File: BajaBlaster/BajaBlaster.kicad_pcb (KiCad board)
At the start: 4 copper layers, 59.2 x 47.5 mm, 51 parts, among them J201 Conn_01x02_Pin, J501 Conn_01x06_Pin, J502 INTERBOARD, J503 Conn_01x04_Pin, SW301 SW_Push, SW302 SW_Push, U201 AP2112K-3.3, U202 TPS562200, U301 ESP32-WROOM-32, U302 MPU-6050, U501 TCAN330

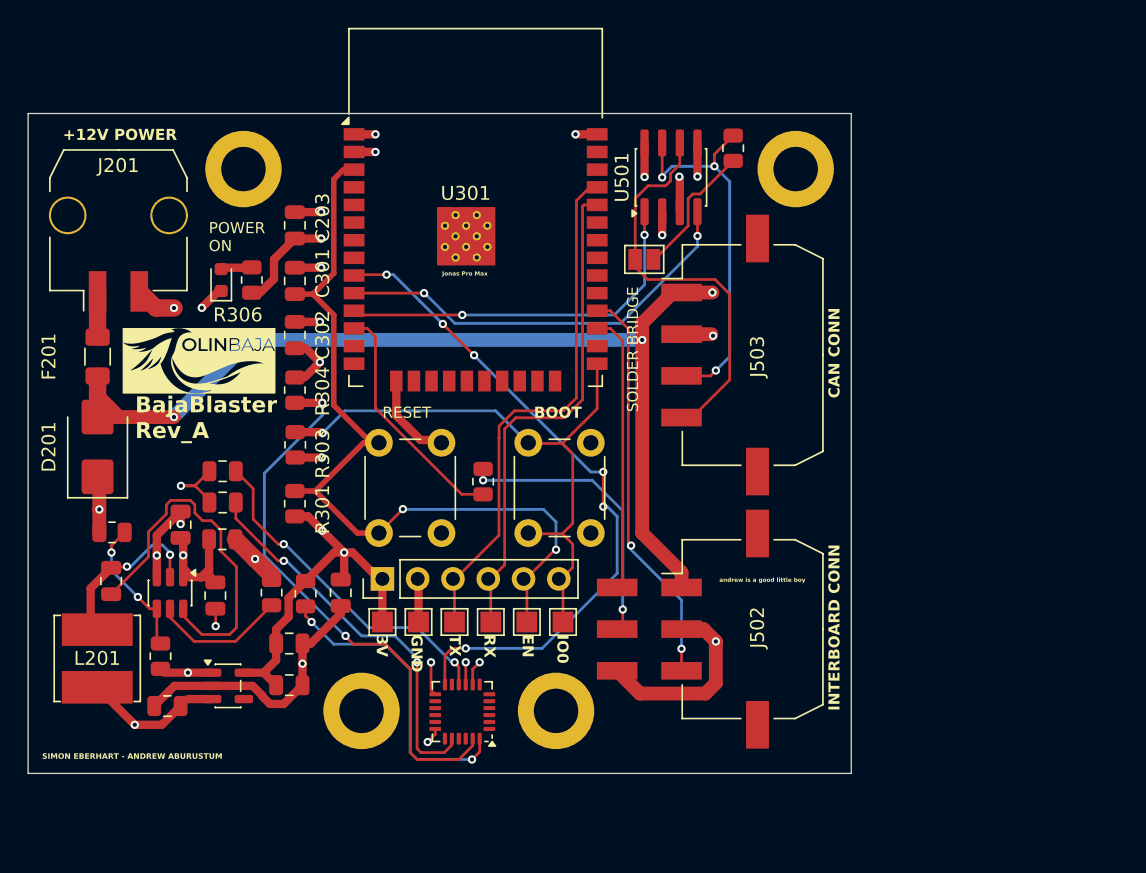
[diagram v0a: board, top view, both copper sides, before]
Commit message: fixed a bunch of smal stuff including changing the cap to be the correct footprint
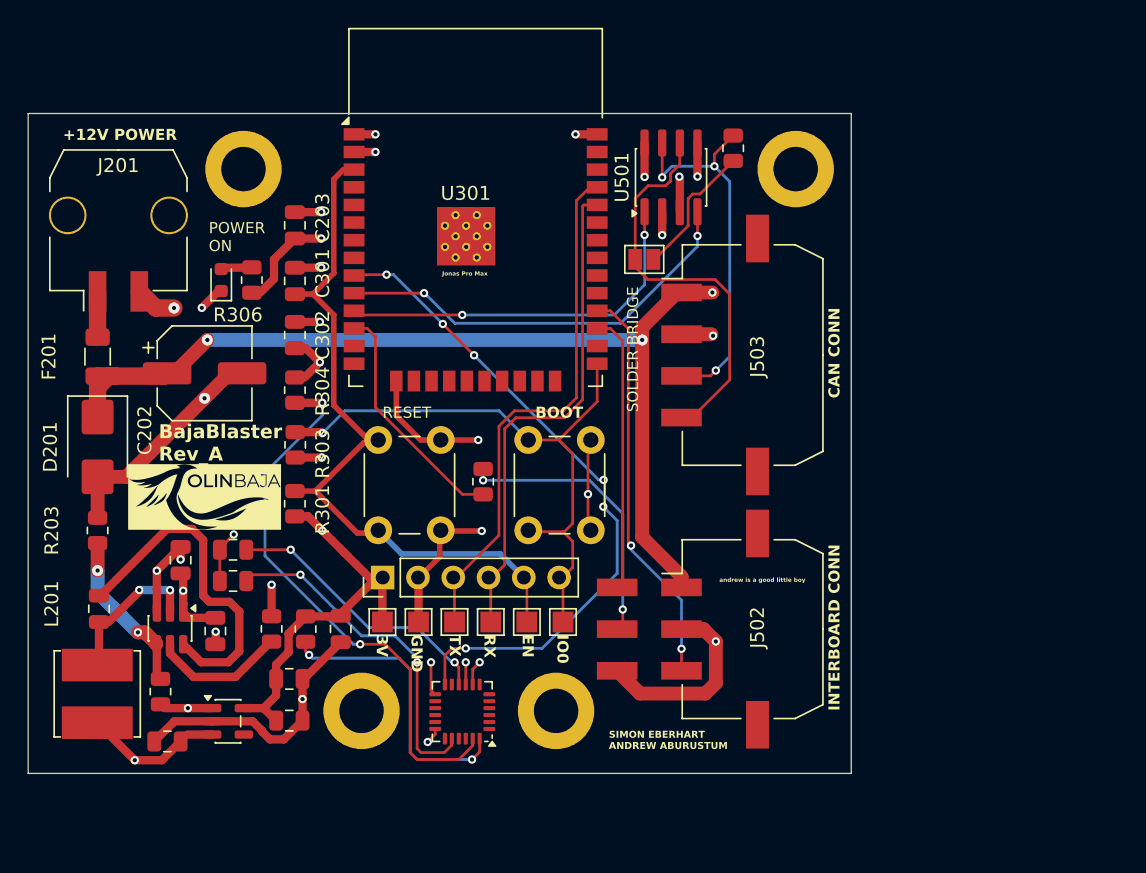
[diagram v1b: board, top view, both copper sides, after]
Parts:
- C202: footprint Capacitor_SMD:C_0805_2012Metric -> Capacitor_SMD:CP_Elec_6.3x7.7
- D201: value SMBJ24A -> SMBJ12A
- L201: value 22uH -> 4.7uH
- moved C202 12.0 mm to (37.7, 93.7)
- moved G*** 9.81 mm to (37.7, 102.6)
- moved C305 5.70 mm to (39.8, 106.4)
- moved C306 5.70 mm to (39.8, 108.7)
- moved R201 2.61 mm to (42.5, 112.1)
- moved C303 2.60 mm to (47.5, 112.1)
- moved C204 2.55 mm to (36.0, 107.2)
- moved L201 2.55 mm to (30.0, 116.8)
- moved C201 2.55 mm to (38.5, 112.2)
- moved C205 2.55 mm to (35.0, 120.2)
- moved C304 2.55 mm to (43.8, 115.7)
- moved C501 2.55 mm to (43.8, 118.7)
- moved R202 2.55 mm to (34.5, 116.6)
- moved R305 2.55 mm to (45.0, 112.1)
- moved U201 2.55 mm to (39.4, 118.8)
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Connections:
- C202 pad 1: GND -> +12V
- C202 pad 2: +12V -> GND
- D201 pad 1: GND -> +12V
- D201 pad 2: +12V -> GND
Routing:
- net GND: track 87.4 -> 109.7 mm, vias 18 -> 21
- net /COMMS/ESP32_EN: track 59.4 -> 54.3 mm, vias 2 -> 0
- net Net-(U302-REGOUT): track 24.5 -> 20.1 mm
- net Net-(U302-CPOUT): track 28.2 -> 24.8 mm
- net +12V: track 82.4 -> 79.2 mm
- net Net-(U202-VFB): track 9.78 -> 11.6 mm
- net +3V3: track 48.6 -> 50.0 mm, vias 9 -> 8
- net Net-(U302-SDA): track 22.2 -> 21.1 mm
- net Net-(U202-VBST): track 25.4 -> 24.7 mm
- net /COMMS/IO0: track 43.7 -> 43.2 mm
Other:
- board text added: "SIMON EBERHART ANDREW ABURUSTUM"
- board text removed: "SIMON EBERHART - ANDREW ABURUSTUM"

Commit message: good for fab
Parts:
- moved C202 0.32 mm to (38.0, 93.6)
- moved D301 0.20 mm to (38.9, 86.8)
- moved R306 0.20 mm to (41.1, 86.8)
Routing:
- net +3V3: track 50.0 -> 50.6 mm
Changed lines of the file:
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@@
 	(footprint "Capacitor_SMD:CP_Elec_6.3x7.7"
 		(layer "F.Cu")
-		(at 37.7 93.7)
+		(at 38 93.6)
 		(descr "SMD capacitor, aluminum electrolytic, Nichicon, 6.3x7.7mm")
 		(tags "capacitor electrolytic")
 		(property "Reference" "C202"
-			(at -4.3 4.1 90)
+			(at -4.5 4.1 90)
 			(layer "F.SilkS")
 			(effects
@@
 	(footprint "Resistor_SMD:R_0805_2012Metric"
 		(layer "F.Cu")
-		(at 41.1 86.9875 90)
+		(at 41.1 86.7875 90)
 		(descr "Resistor SMD 0805 (2012 Metric), square (rectangular) end terminal, IPC-7351 nominal, (Body size source: IPC-SM-782 page 72, https://www.pcb-3d.com/wordpress/wp-content/uploads/ipc-sm-782a_amendment_1_and_2.pdf)")
 		(tags "resistor")
@@
 	(footprint "LED_SMD:LED_0603_1608Metric"
 		(layer "F.Cu")
-		(at 38.9 86.9875 90)
+		(at 38.9 86.7875 90)
 		(descr "LED SMD 0603 (1608 Metric), square (rectangular) end terminal, IPC-7351 nominal, (Body size source: http://www.tortai-tech.com/upload/download/2011102023233369053.pdf)")
 		(tags "LED")
@@
 	)
 	(gr_rect
+		(start 32.199253 104.962389)
+		(end 43.2 105.1)
+		(stroke
+			(width 0)
+			(type solid)
+		)
+		(fill yes)
+		(layer "F.SilkS")
+	)
+	(gr_rect
+		(start 39.912942 100.9)
+		(end 43.076959 101.898755)
+		(stroke
+			(width 0.2)
+			(type solid)
+		)
+		(fill yes)
+		(layer "F.SilkS")
+	)
+	(gr_rect
 		(start 25 75)
 		(end 84.25 122.5)
@@
 	)
 	(segment
+		(start 65.3 103.3)
+		(end 65.3 98.8)
+		(width 0.2)
+		(layer "F.Cu")
+		(net "GND")
+	)
+	(segment
 		(start 38.25 118.75)
 		(end 35.525 118.75)
@@
 	)
 	(segment
+		(start 65.3 105.1)
+		(end 65.3 103.3)
+		(width 0.2)
+		(layer "F.Cu")
+		(net "GND")
+	)
+	(segment
 		(start 34.195 89)
 		(end 33 87.805)
@@
 	)
 	(segment
-		(start 65.3 105.1)
-		(end 65.3 102.4)
-		(width 0.2)
-		(layer "F.Cu")
-		(net "GND")
-	)
-	(segment
 		(start 36.1625 110.25)
 		(end 36.1625 110.2875)
@@
 	)
 	(segment
-		(start 65.3 102.4)
-		(end 65.3 98.8)
-		(width 0.2)
-		(layer "F.Cu")
-		(net "GND")
-	)
-	(segment
 		(start 74.5 116)
 		(end 73.75 116.75)
@@
 	)
 	(segment
+		(start 37.2875 89)
+		(end 38.7125 87.575)
+		(width 0.6)
+		(layer "F.Cu")
+		(net "GND")
+	)
+	(segment
 		(start 38.8 106.3)
 		(end 38.8 106.4)
@@
 	)
 	(segment
-		(start 38.7125 87.775)
-		(end 37.5 88.9875)
-		(width 0.6)
-		(layer "F.Cu")
-		(net "GND")
-	)
-	(segment
 		(start 65.96 76.5)
 		(end 64.4 76.5)
@@
 	)
 	(via
-		(at 37.5 88.9875)
+		(at 37.2875 89)
 		(size 0.6)
 		(drill 0.3)
@@
 	)
 	(via
-		(at 65.3 102.4)
+		(at 65.3 103.3)
 		(size 0.6)
 		(drill 0.3)
@@
 	)
 	(segment
+		(start 42.7 86.9)
+		(end 41.9 87.7)
+		(width 0.6)
+		(layer "F.Cu")
+		(net "+3V3")
+	)
+	(segment
 		(start 45.15 104)
 		(end 46.175 105.025)
@@
 	)
 	(segment
-		(start 44.975 111.244912)
-		(end 44.975 111.2)
+		(start 41.9 87.7)
+		(end 41.1 87.7)
 		(width 0.6)
 		(layer "F.Cu")
@@
 	)
 	(segment
-		(start 41.7 87.9)
-		(end 42.7 86.9)
+		(start 44.975 111.244912)
+		(end 44.975 111.2)
 		(width 0.6)
 		(layer "F.Cu")
@@
 	)
 	(segment
-		(start 34.2625 109.2125)
-		(end 34.275 109.2)
-		(width 0.2)
-		(layer "F.Cu")
-		(net "+12V")
-	)
-	(segment
 		(start 42.525 108.925)
 		(end 42.5 108.9)
@@
 	)
 	(segment
-		(start 39 86.1)
-		(end 41.075 86.1)
+		(start 39 85.9)
+		(end 41.075 85.9)
 		(width 0.6)
 		(layer "F.Cu")
@@
 	)
 	(segment
-		(start 57.75 100.5875)
-		(end 57.75 101.4)
+		(start 57.75 101.384913)
+		(end 57.765087 101.4)
 		(width 0.2)
 		(layer "F.Cu")
@@
 	)
 	(segment
-		(start 57.75 101.4)
+		(start 57.75 101.415087)
 		(end 57.75 101.55)
 		(width 0.2)
@@
 	)
 	(segment
+		(start 57.765087 101.4)
+		(end 57.75 101.415087)
+		(width 0.2)
+		(layer "F.Cu")
+		(net "/COMMS/SYNC")
+	)
+	(segment
+		(start 57.75 100.5875)
+		(end 57.75 101.384913)
+		(width 0.2)
+		(layer "F.Cu")
+		(net "/COMMS/SYNC")
+	)
+	(segment
 		(start 67.8 110.7)
 		(end 67.8 111.715)
@@
 	)
 	(via
-		(at 57.75 101.4)
+		(at 57.765087 101.4)
 		(size 0.6)
 		(drill 0.3)
@@
 	)
 	(segment
-		(start 67.8 110.7)
+		(start 65.4 101.4)
 		(end 67.8 103.8)
 		(width 0.2)
@@
 	)
 	(segment
-		(start 67.8 103.8)
+		(start 57.765087 101.4)
 		(end 65.4 101.4)
 		(width 0.2)
@@
 	)
 	(segment
-		(start 65.4 101.4)
-		(end 57.75 101.4)
+		(start 67.8 103.8)
+		(end 67.8 110.7)
 		(width 0.2)
 		(layer "B.Cu")

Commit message: sendoff
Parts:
- removed R302: 50 OHM, Resistor_SMD:R_0805_2012Metric
- removed SW301, SW302: SW_Push, Button_Switch_THT:SW_PUSH_6mm
- removed U301: ESP32-WROOM-32, RF_Module:ESP32-WROOM-32
- added C302: 10pF, Capacitor_SMD:C_0805_2012Metric, F.Cu at (41.0, 88.5)
- added C303: 100nF, Capacitor_SMD:C_0805_2012Metric, F.Cu at (44.2, 91.0)
- added C307: 10uF, Capacitor_SMD:C_0805_2012Metric, F.Cu at (44.2, 87.0)
- added C308: 100nF, Capacitor_SMD:C_0805_2012Metric, F.Cu at (46.4, 87.0)
- added C309: 100nF, Capacitor_SMD:C_0805_2012Metric, F.Cu at (101.2, 85.8)
- added C310: 10uF, Capacitor_SMD:C_0805_2012Metric, F.Cu at (91.0, 94.0)
- added C311: 100nF, Capacitor_SMD:C_0805_2012Metric, F.Cu at (47.1, 83.6)
- added C312: 4.7uF, Capacitor_SMD:C_0805_2012Metric, F.Cu at (62.8, 94.6)
- added C313: 100nF, Capacitor_SMD:C_0805_2012Metric, F.Cu at (90.2, 101.0)
- added C502: 100nf, Capacitor_SMD:C_0805_2012Metric, F.Cu at (47.4, 95.4)
- added C503: 47pF 50V, Capacitor_SMD:C_0805_2012Metric, F.Cu at (62.8, 88.0)
- added C504: 47pF 50V, Capacitor_SMD:C_0805_2012Metric, F.Cu at (62.8, 85.8)
- added C505: 47pF 50V, Capacitor_SMD:C_0805_2012Metric, F.Cu at (62.8, 83.6)
- added C506: 47pF 50V, Capacitor_SMD:C_0805_2012Metric, F.Cu at (66.7, 89.0)
- added C507: 47pF 50V, Capacitor_SMD:C_0805_2012Metric, F.Cu at (62.8, 90.2)
- added C508: 47pF 50V, Capacitor_SMD:C_0805_2012Metric, F.Cu at (74.8, 78.4)
- added C509: 47pF 50V, Capacitor_SMD:C_0805_2012Metric, F.Cu at (66.7, 111.8)
- added C510: 47pF 50V, Capacitor_SMD:C_0805_2012Metric, F.Cu at (66.7, 109.6)
- added D501: NUP2105L, Package_TO_SOT_SMD:SOT-23, F.Cu at (66.5, 91.8)
- added D502: NUP2105L, Package_TO_SOT_SMD:SOT-23, F.Cu at (66.5, 104.0)
- added FL501: 1812CAN-513NRC, Inductor_SMD:L_CommonModeChoke_Coilcraft_1812CAN, F.Cu at (71.7, 79.3)
- added FL502: 1812CAN-513NRC, Inductor_SMD:L_CommonModeChoke_Coilcraft_1812CAN, F.Cu at (55.0, 79.4)
- added J504: Conn_01x04_Pin, Connector_JST:JST_JWPF_B04B-JWPF-SK-R_1x04_P2.00mm_Vertical, F.Cu at (74.5, 111.0)
- added JP502: SolderJumper_2_Open, Jumper:SolderJumper-2_P1.3mm_Open_Pad1.0x1.5mm, F.Cu at (66.7, 86.6)
- added JP503: JP_EXT_PWR, Jumper:SolderJumper-2_P1.3mm_Open_Pad1.0x1.5mm, F.Cu at (66.7, 84.0)
- added R303: 10kOHM, Resistor_SMD:R_0805_2012Metric, F.Cu at (44.2, 102.8)
- added R309: 10kOHM, Resistor_SMD:R_0805_2012Metric, F.Cu at (44.2, 107.0)
- added R_CAN_TERM502: 120 OHM, Resistor_SMD:R_0805_2012Metric, F.Cu at (66.7, 94.6)
- added SW303: SW_Push, Button_Switch_THT:SW_PUSH_6mm, F.Cu at (48.1, 105.2)
- added SW305: SW_Push, Button_Switch_THT:SW_PUSH_6mm, F.Cu at (55.8, 105.2)
- added U304: STM32F446RETx, Package_QFP:LQFP-64_10x10mm_P0.5mm, F.Cu at (54.2, 89.0)
- added U502: TCAN330, Package_SO:SOIC-8_3.9x4.9mm_P1.27mm, F.Cu at (49.2, 79.6)
- added Y301: 16MHz, Crystal:Crystal_SMD_3225-4Pin_3.2x2.5mm, F.Cu at (36.5, 87.8)
- C301: value 1uF -> 10pF
- J201: footprint Connector_Molex:Molex_Micro-Fit_3.0_43650-0210_1x02-1MP_P3.00mm_Horizontal -> Connector_JST:JST_JWPF_B02B-JWPF-SK-R_1x02_P2.00mm_Vertical
- J502: value INTERBOARD -> Conn_01x04_Pin; footprint Connector_Molex:Molex_Micro-Fit_3.0_43045-0610_2x03-1MP_P3.00mm_Horizontal -> Connector_JST:JST_JWPF_B04B-JWPF-SK-R_1x04_P2.00mm_Vertical
- J503: footprint Connector_Molex:Molex_Micro-Fit_3.0_43650-0412_1x04-1MP_P3.00mm_Horizontal -> Connector_JST:JST_JWPF_B04B-JWPF-SK-R_1x04_P2.00mm_Vertical
- moved C302 44.5 mm to (72.4, 125.4)
- moved REF** 25.0 mm to (65.2, 99.0)
- moved R301 21.5 mm to (62.8, 92.4), turned to 180 degrees
- moved R_CAN_TERM501 17.0 mm to (58.8, 78.2), turned to 0 degrees
- moved J502 14.0 mm to (74.5, 99.0), turned to 0 degrees
- moved JP501 11.5 mm to (58.9, 80.8)
- moved D301 8.45 mm to (30.5, 87.8), turned to -90 degrees
- moved R306 8.16 mm to (33.0, 87.8)
- moved J503 6.20 mm to (74.5, 86.8), turned to 0 degrees
- moved U501 5.55 mm to (65.7, 79.6), turned to 0 degrees
- moved C301 3.45 mm to (41.0, 85.7), turned to 0 degrees
- moved J201 2.33 mm to (32.5, 80.6)
- moved C202 1.50 mm to (36.5, 93.6)
- moved REF** 0.98 mm to (39.6, 79.4)
- moved REF** 0.76 mm to (49.8, 111.8)
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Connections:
- net /COMMS/U0TXD renamed /COMMS/SWDIO
- C201 pad 1: +5V -> EXT_5V_IN
- C205 pad 2: +5V -> EXT_5V_IN
- C301 pad 1: /COMMS/ESP32_EN -> GND
- C301 pad 2: GND -> Net-(U304-PH0)
- J501 pad 4: /COMMS/U0RXD -> /COMMS/SWCLK
- J501 pad 5: /COMMS/ESP32_EN -> /MCU/NRST
- J501 pad 6: /COMMS/IO0 -> /MCU/SWO
- J502 pad 1: +12V -> EXT_5V_IN
- J502 pad 3: /COMMS/INTERBOARD_TX -> /COMMS/INTER_CAN_H
- J502 pad 4: /COMMS/INTERBOARD_RX -> /COMMS/INTER_CAN_L
- J503 pad 1: +12V -> Net-(J503-Pin_1)
- J503 pad 3: /COMMS/CANH -> /COMMS/EXT_CAN_H
- J503 pad 4: /COMMS/CANL -> /COMMS/EXT_CAN_L
- JP501 pad 2: /COMMS/CANL -> /COMMS/INTER_CAN_L
- L201 pad 1: +5V -> EXT_5V_IN
- R202 pad 1: +5V -> EXT_5V_IN
- R301 pad 1: +3V3 -> GND
- R301 pad 2: /COMMS/ESP32_EN -> Net-(U304-PB2)
- R304 pad 1: Net-(U302-SCL) -> /MCU/IMU_SCL
- R305 pad 1: Net-(U302-SDA) -> /MCU/IMU_SDA
- REF** pad 3: /COMMS/U0RXD -> SWDCLK
- REF** pad 4: /COMMS/ESP32_EN -> /MCU/NRST
- REF** pad 5: /COMMS/IO0 -> /MCU/SWO
- R_CAN_TERM501 pad 1: /COMMS/CANH -> /COMMS/INTER_CAN_H
- U201 pad 1: +5V -> EXT_5V_IN
- U201 pad 3: +5V -> EXT_5V_IN
- U302 pad 23: Net-(U302-SCL) -> /MCU/IMU_SCL
- U302 pad 24: Net-(U302-SDA) -> /MCU/IMU_SDA
- U501 pad 1: /COMMS/CAN_TX -> /COMMS/EXT_CAN_TX
- U501 pad 4: /COMMS/CAN_RX -> /COMMS/EXT_CAN_RX
- U501 pad 6: /COMMS/CANL -> /COMMS/EXT_CAN_L_IC
- U501 pad 7: /COMMS/CANH -> /COMMS/EXT_CAN_H_IC
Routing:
- net +12V: track 79.2 -> 20.6 mm, vias 6 -> 4
- net /MCU/IMU_SDA: track 0.00 -> 58.2 mm, vias 0 -> 3
- net /MCU/IMU_SCL: track 0.00 -> 57.5 mm, vias 0 -> 3
- net /COMMS/ESP32_EN: track 54.3 -> 0.00 mm
- net /MCU/NRST: track 0.00 -> 44.4 mm, vias 0 -> 1
- net /COMMS/IO0: track 43.2 -> 1.60 mm
- net Net-(U302-SCL): track 40.2 -> 0.00 mm, vias 2 -> 0
- net /COMMS/U0RXD: track 35.6 -> 0.00 mm
- net /COMMS/SWDIO: track 37.1 -> 2.79 mm
- net /COMMS/EXT_CAN_H: track 0.00 -> 33.5 mm, vias 0 -> 2
- net /MCU/SWO: track 0.00 -> 31.1 mm, vias 0 -> 1
- net /COMMS/CAN_RX: track 30.4 -> 0.00 mm, vias 2 -> 0
- net EXT_5V_IN: track 0.00 -> 30.2 mm, vias 0 -> 4
- net /COMMS/CANL: track 29.3 -> 0.00 mm
- net /COMMS/INTERBOARD_TX: track 29.1 -> 0.00 mm, vias 2 -> 0
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- added copper zone on In2.Cu, net EXT_5V_IN
- removed copper zone on In2.Cu, net +5V
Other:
- board size 59.2 x 47.5 mm -> 53.8 x 47.5 mm
- board text added: "CLK"
- board text added: "IO"
- board text added: "NRST"
- board text added: "SWO"
- board text removed: "EN"
- board text removed: "IO0"
- board text removed: "Jonas Pro Max"
- board text removed: "POWER ON"
- board text removed: "RX"
- board text removed: "SIMON EBERHART ANDREW ABURUSTUM"
- board text removed: "SOLDER BRIDGE"
- board text removed: "TX"
- board text removed: "andrew is a good little boy"
